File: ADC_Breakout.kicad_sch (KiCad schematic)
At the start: 29 parts, among them J1 Analog Pins, J2 Digital Power, J3 Clock Chooser, J4 Analog Power, J5 SPI Communication, SW0 SW_Push, U2 SN74AUP2G80DCUR, X1 SIT8924BA-22-33E-8.192000, Y1 Crystal_Small

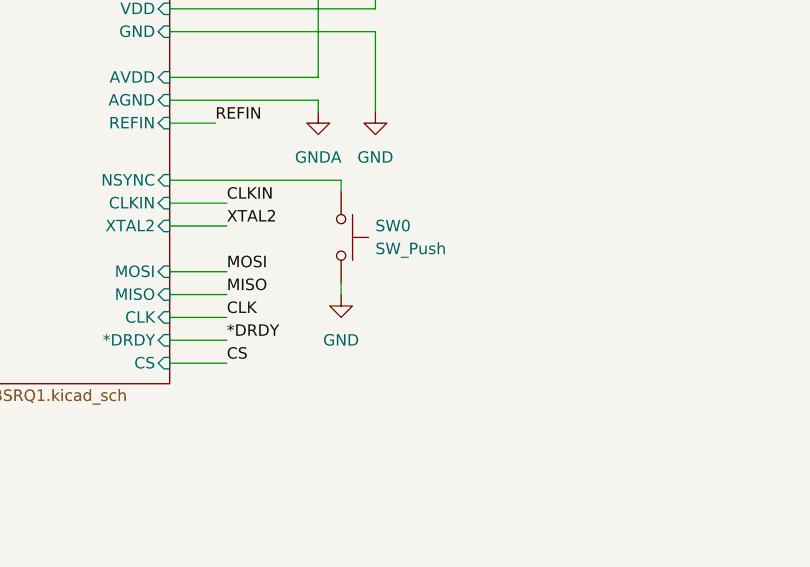
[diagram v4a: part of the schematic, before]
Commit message: New footprints added
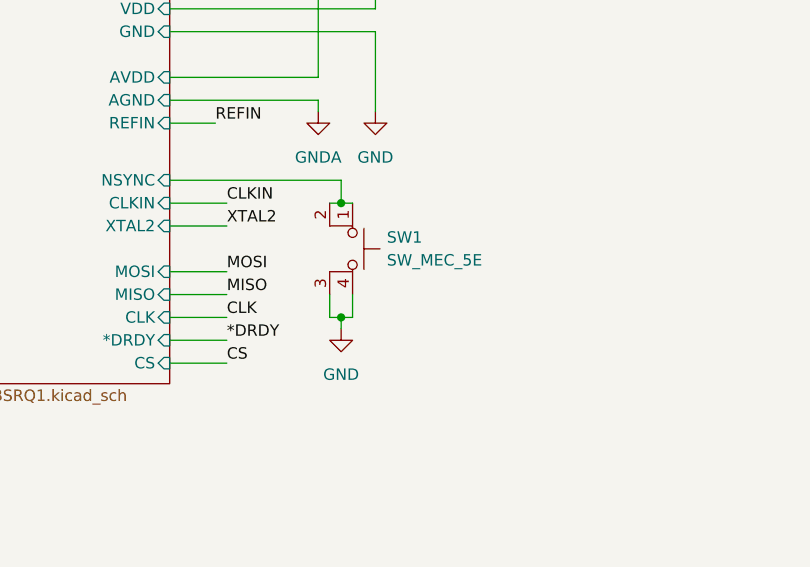
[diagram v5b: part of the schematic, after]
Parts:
- removed SW0: SW_Push, symbol Switch:SW_Push
- added SW1: SW_MEC_5E, symbol Switch:SW_MEC_5E
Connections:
- net ADC/NSYNC: now also SW1.1, SW1.2
- net GND: now also SW1.3 (K), SW1.4 (A)
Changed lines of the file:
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@@
 	)
 	(junction
+		(at 232.41 74.93)
+		(diameter 0)
+		(color 0 0 0 0)
+	)
+	(junction
 		(at 106.68 72.39)
 		(diameter 0)
@@
 	)
 	(junction
+		(at 232.41 62.23)
+		(diameter 0)
+		(color 0 0 0 0)
+	)
+	(junction
 		(at 38.1 92.71)
 		(diameter 0)
@@
 	(wire
 		(pts
+			(xy 231.14 62.23) (xy 232.41 62.23)
+		)
+		(stroke
+			(width 0)
+			(type default)
+		)
+	)
+	(wire
+		(pts
 			(xy 40.64 140.97) (xy 43.18 140.97)
 		)
@@
 	(wire
 		(pts
-			(xy 232.41 71.12) (xy 232.41 72.39)
+			(xy 232.41 74.93) (xy 232.41 76.2)
 		)
 		(stroke
@@
 	(wire
 		(pts
-			(xy 232.41 59.69) (xy 232.41 60.96)
+			(xy 49.53 143.51) (xy 46.99 143.51)
 		)
 		(stroke
@@
 	(wire
 		(pts
-			(xy 49.53 143.51) (xy 46.99 143.51)
+			(xy 106.68 67.31) (xy 106.68 69.85)
 		)
 		(stroke
@@
 	(wire
 		(pts
-			(xy 106.68 67.31) (xy 106.68 69.85)
+			(xy 229.87 50.8) (xy 229.87 52.07)
 		)
 		(stroke
@@
 	(wire
 		(pts
-			(xy 229.87 50.8) (xy 229.87 52.07)
+			(xy 232.41 62.23) (xy 233.68 62.23)
 		)
 		(stroke
@@
 	(wire
 		(pts
+			(xy 231.14 72.39) (xy 231.14 74.93)
+		)
+		(stroke
+			(width 0)
+			(type default)
+		)
+	)
+	(wire
+		(pts
+			(xy 233.68 72.39) (xy 233.68 74.93)
+		)
+		(stroke
+			(width 0)
+			(type default)
+		)
+	)
+	(wire
+		(pts
+			(xy 232.41 59.69) (xy 232.41 62.23)
+		)
+		(stroke
+			(width 0)
+			(type default)
+		)
+	)
+	(wire
+		(pts
 			(xy 97.79 176.53) (xy 100.33 176.53)
 		)
@@
 	(wire
 		(pts
+			(xy 233.68 74.93) (xy 232.41 74.93)
+		)
+		(stroke
+			(width 0)
+			(type default)
+		)
+	)
+	(wire
+		(pts
 			(xy 43.18 152.4) (xy 46.99 152.4)
 		)
@@
 	(wire
 		(pts
+			(xy 231.14 74.93) (xy 232.41 74.93)
+		)
+		(stroke
+			(width 0)
+			(type default)
+		)
+	)
+	(wire
+		(pts
 			(xy 203.2 138.43) (xy 209.55 138.43)
 		)
@@
 	)
 	(symbol
-		(lib_id "Switch:SW_Push")
-		(at 232.41 66.04 270)
+		(lib_id "power:VDD")
+		(at 241.3 123.19 0)
 		(unit 1)
 		(exclude_from_sim no)
@@
 		(dnp no)
 		(fields_autoplaced yes)
-		(property "Reference" "SW0"
-			(at 236.22 64.7699 90)
+		(property "Reference" "#PWR021"
+			(at 241.3 127 0)
 			(effects
 				(font
 					(size 1.27 1.27)
 				)
-				(justify left)
+				(hide yes)
 			)
 		)
-		(property "Value" "SW_Push"
-			(at 236.22 67.3099 90)
+		(property "Value" "VDD"
+			(at 241.3 118.11 0)
 			(effects
 				(font
 					(size 1.27 1.27)
 				)
-				(justify left)
 			)
 		)
 		(property "Footprint" ""
-			(at 237.49 66.04 0)
+			(at 241.3 123.19 0)
 			(effects
 				(font
@@
 			)
 		)
-		(property "Datasheet" "~"
-			(at 237.49 66.04 0)
+		(property "Datasheet" ""
+			(at 241.3 123.19 0)
 			(effects
 				(font
@@
 			)
 		)
-		(property "Description" "Push button switch, generic, two pins"
-			(at 232.41 66.04 0)
+		(property "Description" "Power symbol creates a global label with name \"VDD\""
+			(at 241.3 123.19 0)
 			(effects
 				(font
@@
 		(pin "1"
 		)
-		(pin "2"
-		)
 		(instances
 			(project ""
 				(path "/9e6f337e-b8cc-44e4-808a-ba1b350193a1"
-					(reference "SW0")
+					(reference "#PWR021")
 					(unit 1)
 				)
@@
 	)
 	(symbol
-		(lib_id "power:VDD")
-		(at 241.3 123.19 0)
+		(lib_id "Connector:TestPoint")
+		(at 34.29 81.28 0)
 		(unit 1)
 		(exclude_from_sim no)
@@
 		(on_board yes)
 		(dnp no)
-		(fields_autoplaced yes)
-		(property "Reference" "#PWR021"
-			(at 241.3 127 0)
+		(property "Reference" "TP1"
+			(at 31.75 76.7079 0)
 			(effects
 				(font
 					(size 1.27 1.27)
 				)
-				(hide yes)
+				(justify right)
 			)
 		)
-		(property "Value" "VDD"
-			(at 241.3 118.11 0)
+		(property "Value" "TestPoint"
+			(at 31.75 79.2479 0)
 			(effects
 				(font
 					(size 1.27 1.27)
 				)
+				(justify right)
 			)
 		)
-		(property "Footprint" ""
-			(at 241.3 123.19 0)
+		(property "Footprint" "SVT_Special:TestPoint_HEX_3mmID"
+			(at 39.37 81.28 0)
 			(effects
 				(font
@@
 			)
 		)
-		(property "Datasheet" ""
-			(at 241.3 123.19 0)
+		(property "Datasheet" "~"
+			(at 39.37 81.28 0)
 			(effects
 				(font
@@
 			)
 		)
-		(property "Description" "Power symbol creates a global label with name \"VDD\""
-			(at 241.3 123.19 0)
+		(property "Description" "test point"
+			(at 34.29 81.28 0)
 			(effects
 				(font
@@
 			(project ""
 				(path "/9e6f337e-b8cc-44e4-808a-ba1b350193a1"
-					(reference "#PWR021")
+					(reference "TP1")
 					(unit 1)
 				)
@@
 	)
 	(symbol
-		(lib_id "Connector:TestPoint")
-		(at 34.29 81.28 0)
+		(lib_id "Switch:SW_MEC_5E")
+		(at 231.14 67.31 270)
 		(unit 1)
 		(exclude_from_sim no)
@@
 		(on_board yes)
 		(dnp no)
-		(property "Reference" "TP1"
-			(at 31.75 76.7079 0)
+		(fields_autoplaced yes)
+		(property "Reference" "SW1"
+			(at 237.49 66.0399 90)
 			(effects
 				(font
 					(size 1.27 1.27)
 				)
-				(justify right)
+				(justify left)
 			)
 		)
-		(property "Value" "TestPoint"
-			(at 31.75 79.2479 0)
+		(property "Value" "SW_MEC_5E"
+			(at 237.49 68.5799 90)
 			(effects
 				(font
 					(size 1.27 1.27)
 				)
-				(justify right)
+				(justify left)
 			)
 		)
-		(property "Footprint" "SVT_Special:TestPoint_HEX_3mmID"
-			(at 39.37 81.28 0)
+		(property "Footprint" ""
+			(at 238.76 67.31 0)
 			(effects
 				(font
@@
 			)
 		)
-		(property "Datasheet" "~"
-			(at 39.37 81.28 0)
+		(property "Datasheet" "http://www.apem.com/int/index.php?controller=attachment&id_attachment=1371"
+			(at 238.76 67.31 0)
 			(effects
 				(font
@@
 			)
 		)
-		(property "Description" "test point"
-			(at 34.29 81.28 0)
+		(property "Description" "MEC 5E single pole normally-open tactile switch"
+			(at 231.14 67.31 0)
 			(effects
 				(font
@@
 		(pin "1"
 		)
+		(pin "3"
+		)
+		(pin "4"
+		)
+		(pin "2"
+		)
 		(instances
 			(project ""
 				(path "/9e6f337e-b8cc-44e4-808a-ba1b350193a1"
-					(reference "TP1")
+					(reference "SW1")
 					(unit 1)
 				)
@@
 	(symbol
 		(lib_id "power:GND")
-		(at 232.41 72.39 0)
+		(at 232.41 76.2 0)
 		(unit 1)
 		(exclude_from_sim no)
@@
 		(fields_autoplaced yes)
 		(property "Reference" "#PWR03"
-			(at 232.41 78.74 0)
+			(at 232.41 82.55 0)
 			(effects
 				(font
@@
 		)
 		(property "Value" "GND"
-			(at 232.41 77.47 0)
+			(at 232.41 81.28 0)
 			(effects
 				(font
@@
 		)
 		(property "Footprint" ""
-			(at 232.41 72.39 0)
+			(at 232.41 76.2 0)
 			(effects
 				(font
@@
 		)
 		(property "Datasheet" ""
-			(at 232.41 72.39 0)
+			(at 232.41 76.2 0)
 			(effects
 				(font
@@
 		)
 		(property "Description" "Power symbol creates a global label with name \"GND\" , ground"
-			(at 232.41 72.39 0)
+			(at 232.41 76.2 0)
 			(effects
 				(font

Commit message: added all files
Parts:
- SW1: footprint (none) -> SMD_Button:SW_B3SL-1002P_OMR
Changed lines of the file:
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@@
 			)
 		)
-		(property "Footprint" ""
+		(property "Footprint" "SMD_Button:SW_B3SL-1002P_OMR"
 			(at 238.76 67.31 0)
 			(effects

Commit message: Updated Layout
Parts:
- removed J1: Analog Pins, Connector_PinHeader_2.54mm:PinHeader_2x08_P2.54mm_Vertical, symbol Connector_Generic:Conn_02x08_Odd_Even
- removed J5: SPI Communication, Connector_PinHeader_2.54mm:PinHeader_1x05_P2.54mm_Vertical, symbol Connector_Generic:Conn_01x05
- added J0: Conn_01x06, Connector_PinHeader_2.54mm:PinHeader_1x06_P2.54mm_Vertical, symbol Connector_Generic:Conn_01x06
- added J10, J11, J12, J13, J6, J7, J8, J9: Conn_01x02, Connector_PinHeader_2.54mm:PinHeader_1x02_P2.54mm_Vertical, symbol Connector_Generic:Conn_01x02
- D0: footprint (none) -> Capacitor_SMD:C_0603_1608Metric_Pad1.08x0.95mm_HandSolder
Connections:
- net *DRDY: now also J0.5 (Pin_5)
- net A0_N: now also J6.2 (Pin_2)
- net A0_P: now also J6.1 (Pin_1)
- net A1_N: now also J7.2 (Pin_2)
- net A1_P: now also J7.1 (Pin_1)
- net A2_N: now also J8.2 (Pin_2)
- net A2_P: now also J8.1 (Pin_1)
- net A3_N: now also J9.2 (Pin_2)
- net A3_P: now also J9.1 (Pin_1)
- net A4_N: now also J10.2 (Pin_2)
- net A4_P: now also J10.1 (Pin_1)
- net A5_N: now also J11.2 (Pin_2)
- net A5_P: now also J11.1 (Pin_1)
- net A6_N: now also J12.2 (Pin_2)
- net A6_P: now also J12.1 (Pin_1)
- net A7_N: now also J13.2 (Pin_2)
- net A7_P: now also J13.1 (Pin_1)
- net CLK: now also J0.4 (Pin_4)
- net CS: now also J0.6 (Pin_6)
- net GND: now also J0.1 (Pin_1)
- net MISO: now also J0.3 (Pin_3)
- net MOSI: now also J0.2 (Pin_2)

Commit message: Added graphics + iBOM
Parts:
- added LOGO0: LHRs, Top:LHRs_LOGO, symbol UTSVT_Misc:Logo_Placeholder
- added LOGO1: UTSVT Logo, SVT_Special:UTSVT_Logo_Symbol, symbol UTSVT_Misc:Logo_Placeholder
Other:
- note added: "Graphics"
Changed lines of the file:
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@@
 	)
 	(rectangle
+		(start 125.476 109.982)
+		(end 177.038 165.862)
+		(stroke
+			(width 0)
+			(type default)
+		)
+		(fill
+			(type none)
+		)
+	)
+	(rectangle
 		(start 11.938 122.682)
 		(end 125.476 198.12)
@@
 		)
 	)
+	(text "Graphics"
+		(exclude_from_sim no)
+		(at 149.606 150.622 0)
+		(effects
+			(font
+				(size 1.27 1.27)
+			)
+		)
+	)
 	(text "External Oscillator\nChosen from TI Development Board"
 		(exclude_from_sim no)
@@
 	)
 	(symbol
+		(lib_id "UTSVT_Misc:Logo_Placeholder")
+		(at 144.78 124.46 0)
+		(unit 1)
+		(exclude_from_sim no)
+		(in_bom yes)
+		(on_board yes)
+		(dnp no)
+		(fields_autoplaced yes)
+		(property "Reference" "LOGO0"
+			(at 144.78 120.65 0)
+			(effects
+				(font
+					(size 1.27 1.27)
+				)
+				(hide yes)
+			)
+		)
+		(property "Value" "LHRs"
+			(at 148.59 124.4599 0)
+			(effects
+				(font
+					(size 1.27 1.27)
+				)
+				(justify left)
+			)
+		)
+		(property "Footprint" "Top:LHRs_LOGO"
+			(at 144.78 122.555 0)
+			(effects
+				(font
+					(size 1.27 1.27)
+				)
+				(hide yes)
+			)
+		)
+		(property "Datasheet" ""
+			(at 144.78 122.555 0)
+			(effects
+				(font
+					(size 1.27 1.27)
+				)
+				(hide yes)
+			)
+		)
+		(property "Description" "Graph footprint placeholder"
+			(at 144.78 124.46 0)
+			(effects
+				(font
+					(size 1.27 1.27)
+				)
+				(hide yes)
+			)
+		)
+		(instances
+			(project ""
+				(path "/9e6f337e-b8cc-44e4-808a-ba1b350193a1"
+					(reference "LOGO0")
+					(unit 1)
+				)
+			)
+		)
+	)
+	(symbol
 		(lib_id "power:GND")
 		(at 236.22 52.07 0)
@@
 					(unit 1)
 				)
+			)
+		)
+	)
+	(symbol
+		(lib_id "UTSVT_Misc:Logo_Placeholder")
+		(at 144.78 134.62 0)
+		(unit 1)
+		(exclude_from_sim no)
+		(in_bom yes)
+		(on_board yes)
+		(dnp no)
+		(fields_autoplaced yes)
+		(property "Reference" "LOGO1"
+			(at 144.78 130.81 0)
+			(effects
+				(font
+					(size 1.27 1.27)
+				)
+				(hide yes)
+			)
+		)
+		(property "Value" "UTSVT Logo"
+			(at 148.59 134.6199 0)
+			(effects
+				(font
+					(size 1.27 1.27)
+				)
+				(justify left)
+			)
+		)
+		(property "Footprint" "SVT_Special:UTSVT_Logo_Symbol"
+			(at 144.78 132.715 0)
+			(effects
+				(font
+					(size 1.27 1.27)
+				)
+				(hide yes)
+			)
+		)
+		(property "Datasheet" ""
+			(at 144.78 132.715 0)
+			(effects
+				(font
+					(size 1.27 1.27)
+				)
+				(hide yes)
+			)
+		)
+		(property "Description" "Graph footprint placeholder"
+			(at 144.78 134.62 0)
+			(effects
+				(font
+					(size 1.27 1.27)
+				)
+				(hide yes)
+			)
+		)
+		(instances
+			(project "ADC_Breakout"
+				(path "/9e6f337e-b8cc-44e4-808a-ba1b350193a1"
+					(reference "LOGO1")
+					(unit 1)
+				)
